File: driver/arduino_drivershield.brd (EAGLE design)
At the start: 59.7 x 54.3 mm, 35 parts, among them IC1 LB1973M, IC10 LB1973M, IC11 LB1973M, IC12 74HC14D, IC2 LB1973M, IC3 74HC14D, IC4 LB1973M, IC5 LB1973M, IC6 74HC14D, IC7 LB1973M, IC8 LB1973M, IC9 74HC14D, J1 J5MM, J2 J5MM, U1 ARDUINO_SHIELDLABEL

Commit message: autorouted
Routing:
- net V+: track 0.00 -> 136.5 mm
- net GND@2: track 11.9 -> 126.5 mm
- net GND@3: track 0.00 -> 108.7 mm
- net 5V@1: track 0.00 -> 104.2 mm, vias 0 -> 2
- net 5V: track 0.00 -> 93.3 mm, vias 0 -> 2
- net N$28: track 0.00 -> 81.6 mm, vias 0 -> 1
- net N$51: track 0.00 -> 77.6 mm, vias 0 -> 2
- net TX: track 0.00 -> 29.0 mm
- net RX: track 0.00 -> 29.0 mm
- net N$15: track 0.00 -> 23.9 mm, vias 0 -> 1
- net N$16: track 0.00 -> 23.9 mm, vias 0 -> 1
- net N$35: track 0.00 -> 22.7 mm, vias 0 -> 1
- net N$36: track 0.00 -> 22.4 mm, vias 0 -> 1
- net N$66: track 0.00 -> 20.6 mm
- net N$50: track 0.00 -> 20.6 mm
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
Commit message: seems I forgot to save the last routing
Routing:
- net GND@2: track 126.5 -> 108.2 mm
- net N$28: track 81.6 -> 73.0 mm
- net N$38: track 15.0 -> 12.0 mm
- net N$50: track 20.6 -> 18.0 mm, vias 0 -> 1
- net N$51: track 77.6 -> 79.1 mm
- net 5V: track 93.3 -> 92.7 mm

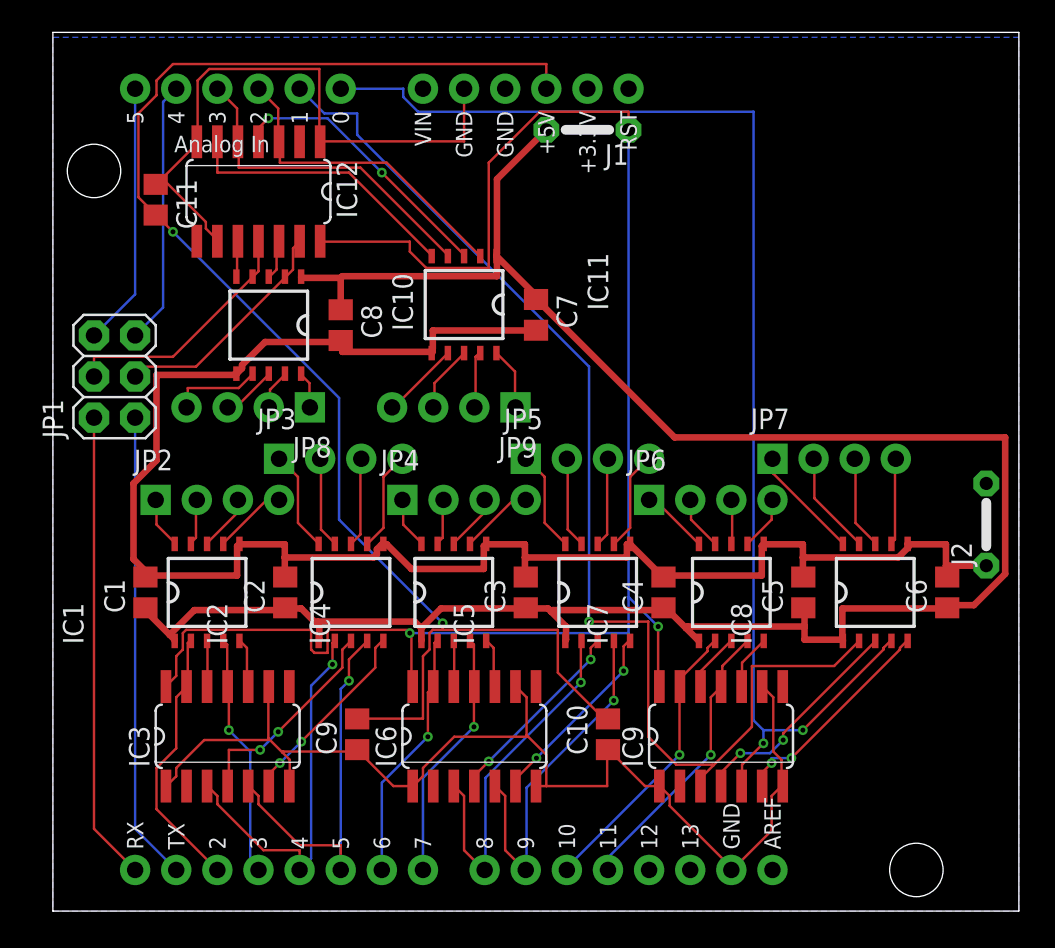
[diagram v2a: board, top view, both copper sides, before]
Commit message: added some more jumper to hopefully get better ground connections
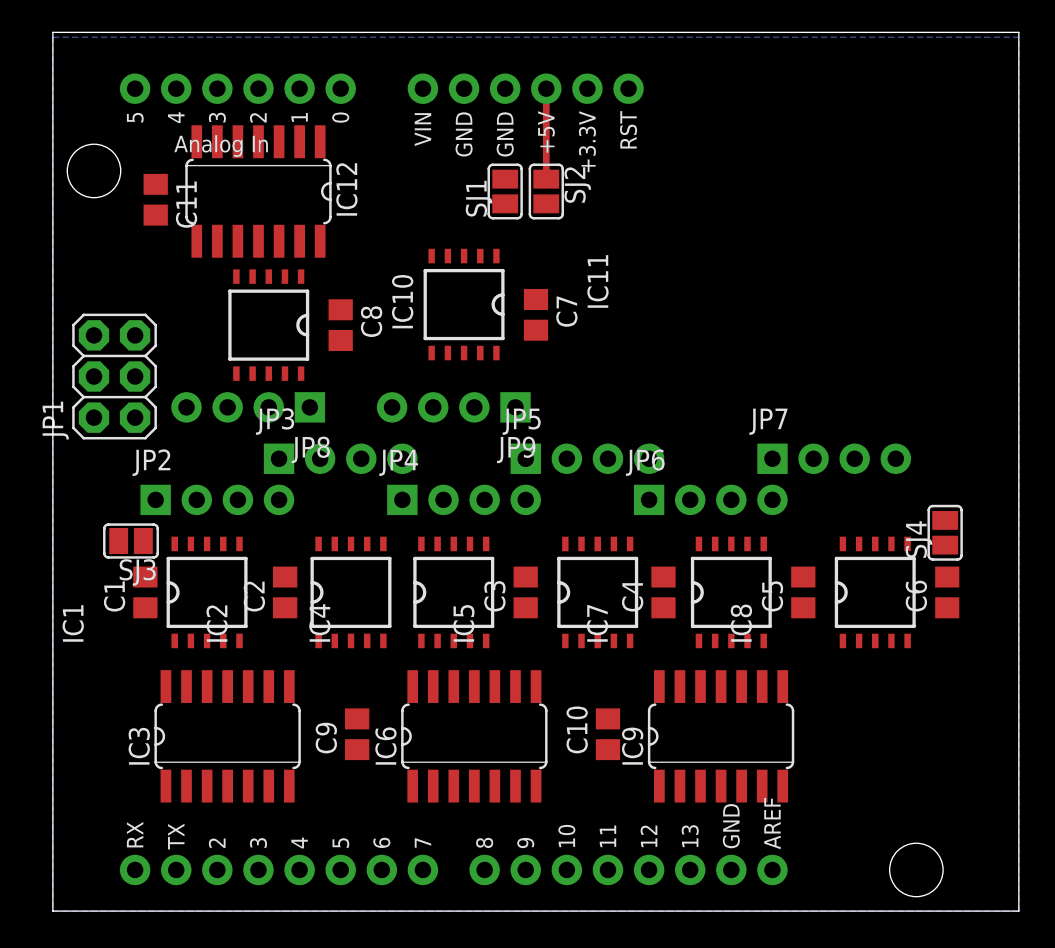
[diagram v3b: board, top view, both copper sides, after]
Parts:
- removed J1, J2: J5MM, jumper:05
- added SJ1, SJ2, SJ3, SJ4: (no value), jumper:SJ
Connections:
- removed net GND@2: C10.1, C11.1, C9.1, IC12.1, IC12.7, IC12.9, IC3.1, IC3.7, IC3.9, IC6.1, IC6.7, IC6.9, IC9.1, IC9.7, IC9.9, J2.2, U1.GND@0, U1.GND@1, U1.GND@2
- removed net GND@3: C1.2, C2.2, C3.2, C4.2, C5.2, C6.2, C7.2, C8.2, IC1.6, IC10.6, IC11.6, IC2.6, IC4.6, IC5.6, IC7.6, IC8.6, J2.1
- new net FOO: C1.2, C2.2, C3.2, C4.2, C5.2, C6.2, C7.2, C8.2, IC1.6, IC11.6, IC2.6, IC4.6, IC5.6, IC7.6, IC8.6, SJ1.1, SJ3.1, SJ4.1
- new net GND: C10.1, C11.1, C9.1, IC12.1, IC12.7, IC12.9, IC3.1, IC3.7, IC3.9, IC6.1, IC6.7, IC6.9, IC9.1, IC9.7, IC9.9, SJ1.2, U1.GND@0, U1.GND@1, U1.GND@2
- new net GND@PWR: IC10.6
- net 5V: now also SJ2.1
- net 5V@1: no longer J1.1
- net V+: now also SJ2.2; no longer J1.2
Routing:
- net V+: track 136.5 -> 0.00 mm
- net GND@3: track 108.7 -> 0.00 mm
- net GND@2: track 108.2 -> 0.00 mm
- net 5V@1: track 104.2 -> 0.00 mm, vias 2 -> 0
- net 5V: track 92.7 -> 5.59 mm, vias 2 -> 0
- net N$51: track 79.1 -> 0.00 mm, vias 2 -> 0
- net N$28: track 73.0 -> 0.00 mm, vias 1 -> 0
- net TX: track 29.0 -> 0.00 mm
- net RX: track 29.0 -> 0.00 mm
- net N$15: track 23.9 -> 0.00 mm, vias 1 -> 0
- net N$16: track 23.9 -> 0.00 mm, vias 1 -> 0
- net N$35: track 22.7 -> 0.00 mm, vias 1 -> 0
- net N$36: track 22.4 -> 0.00 mm, vias 1 -> 0
- net N$66: track 20.6 -> 0.00 mm
- net N$30: track 19.9 -> 0.00 mm
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- added copper zone on layer 16, net GND
- removed copper zone on layer 16, net GND@2

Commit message: thicker trace from 5V to power net v+, better placement for one jumper
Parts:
- moved SJ1 11.0 mm to (30.7, 33.8), turned to 0 degrees
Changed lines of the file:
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@@
 <element name="C10" library="rcl" package="C0805" value="" x="34.29" y="10.922" rot="R90"/>
 <element name="C11" library="rcl" package="C0805" value="" x="6.35" y="43.942" rot="R270"/>
-<element name="SJ1" library="jumper" package="SJ" value="" x="27.94" y="44.45" rot="R90"/>
+<element name="SJ1" library="jumper" package="SJ" value="" x="30.734" y="33.782"/>
 <element name="SJ2" library="jumper" package="SJ" value="" x="30.48" y="44.45" rot="R270"/>
 <element name="SJ3" library="jumper" package="SJ" value="" x="4.826" y="22.86" rot="R180"/>
@@
 <wire x1="17.78" y1="35.245" x2="23.4" y2="34.469" width="0" layer="19" extent="1-1"/>
 <wire x1="29.845" y1="35.88" x2="23.4" y2="34.469" width="0" layer="19" extent="1-1"/>
-<wire x1="27.94" y1="43.688" x2="29.845" y2="35.88" width="0" layer="19" extent="1-1"/>
+<wire x1="29.972" y1="33.782" x2="29.845" y2="35.88" width="0" layer="19" extent="1-1"/>
 </signal>
 <signal name="GND">
@@
 <contactref element="C11" pad="1"/>
 <contactref element="SJ1" pad="2"/>
-<wire x1="27.94" y1="50.8" x2="27.94" y2="45.212" width="0" layer="19" extent="1-1"/>
+<wire x1="27.94" y1="50.8" x2="31.496" y2="33.782" width="0" layer="19" extent="1-1"/>
 <wire x1="45.085" y1="7.7216" x2="41.91" y2="2.54" width="0" layer="19" extent="1-1"/>
 <wire x1="43.815" y1="13.8684" x2="45.085" y2="7.7216" width="0" layer="19" extent="1-1"/>
@@
 <wire x1="18.796" y1="11.872" x2="6.35" y2="42.992" width="0" layer="19" extent="1-1"/>
 <wire x1="34.29" y1="11.872" x2="18.796" y2="11.872" width="0" layer="19" extent="1-1"/>
-<wire x1="30.48" y1="50.8" x2="30.48" y2="45.212" width="0.4064" layer="1"/>
+<wire x1="30.48" y1="50.8" x2="30.48" y2="45.212" width="0.6096" layer="1"/>
 </signal>
 <signal name="GND@PWR" class="1">

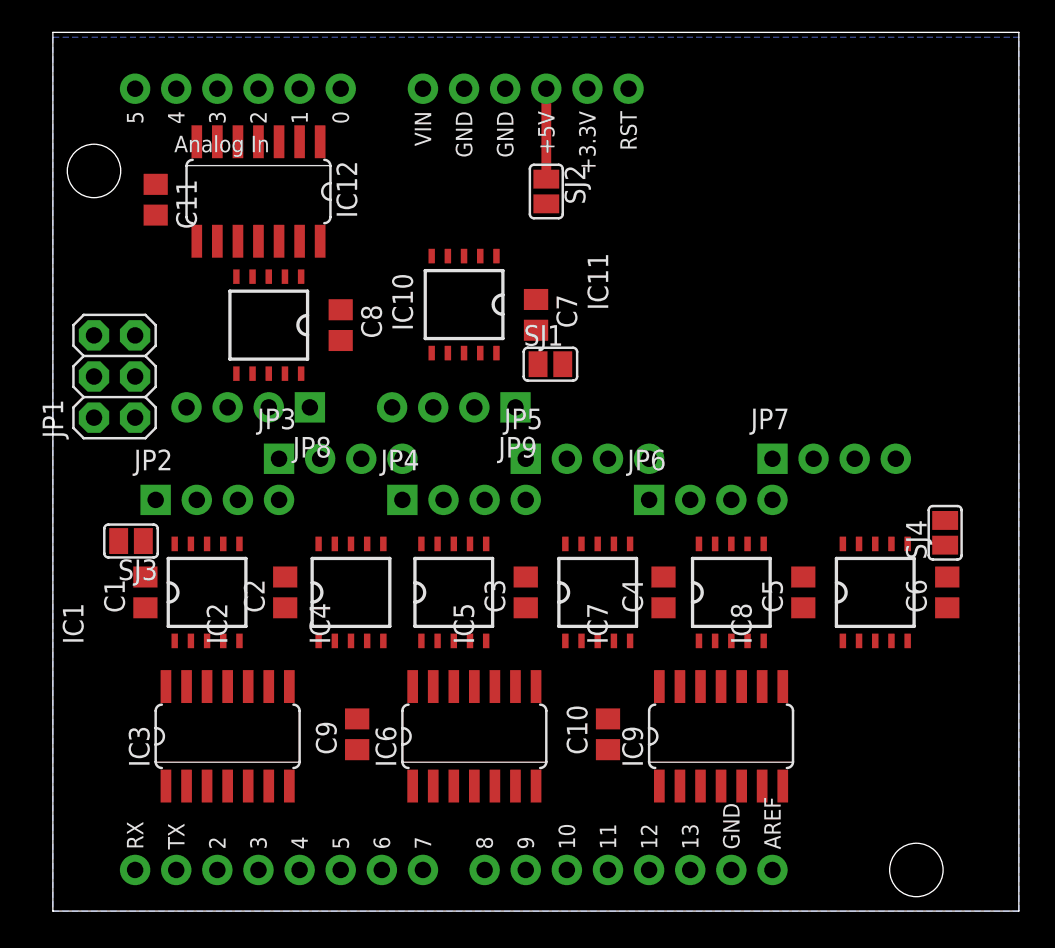
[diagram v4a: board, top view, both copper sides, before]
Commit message: realized the GND jumpers should probably be at bottom side
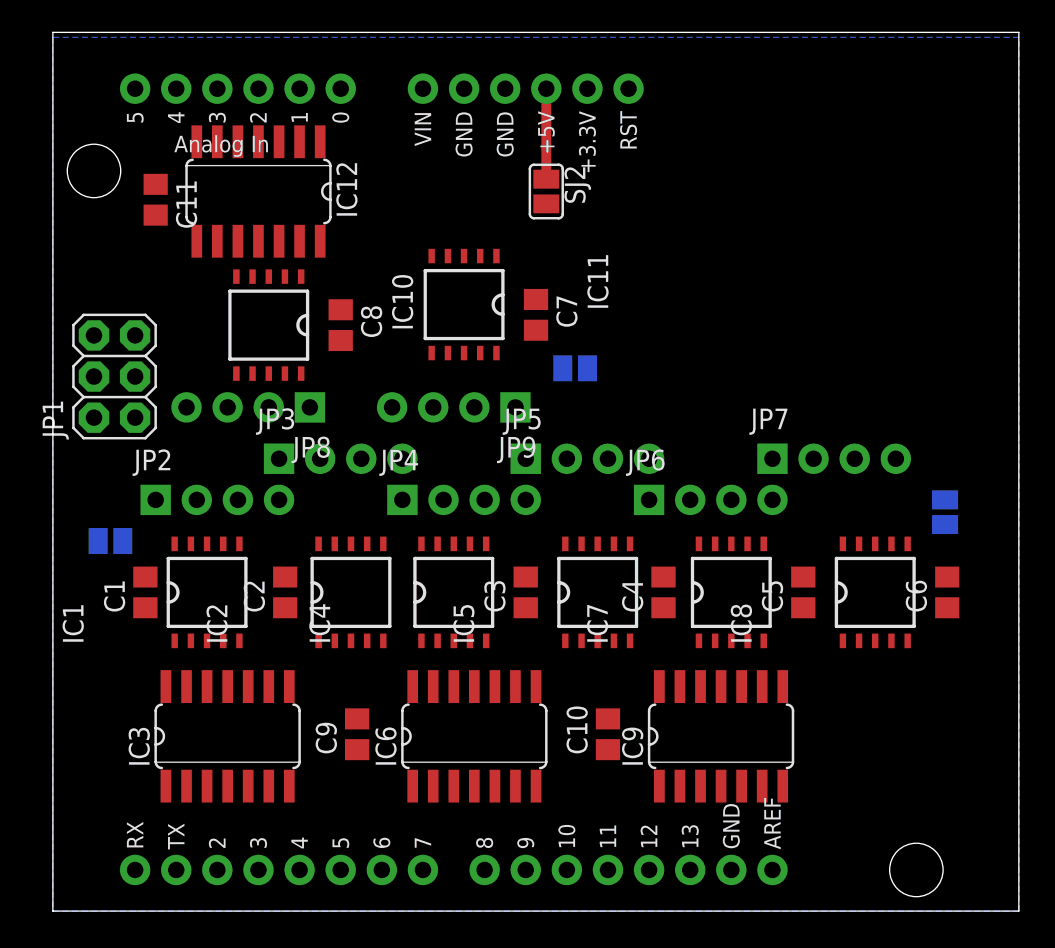
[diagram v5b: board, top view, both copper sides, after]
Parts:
- moved SJ1 1.55 mm to (32.3, 33.5), flipped to the bottom, turned to 180 degrees
- moved SJ4 1.27 mm to (55.1, 24.6), flipped to the bottom
- moved SJ3 1.27 mm to (3.56, 22.9), flipped to the bottom, turned to 0 degrees
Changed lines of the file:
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@@
 <element name="C10" library="rcl" package="C0805" value="" x="34.29" y="10.922" rot="R90"/>
 <element name="C11" library="rcl" package="C0805" value="" x="6.35" y="43.942" rot="R270"/>
-<element name="SJ1" library="jumper" package="SJ" value="" x="30.734" y="33.782"/>
+<element name="SJ1" library="jumper" package="SJ" value="" x="32.258" y="33.528" rot="MR180"/>
 <element name="SJ2" library="jumper" package="SJ" value="" x="30.48" y="44.45" rot="R270"/>
-<element name="SJ3" library="jumper" package="SJ" value="" x="4.826" y="22.86" rot="R180"/>
-<element name="SJ4" library="jumper" package="SJ" value="" x="55.118" y="23.368" rot="R90"/>
+<element name="SJ3" library="jumper" package="SJ" value="" x="3.556" y="22.86" rot="MR0"/>
+<element name="SJ4" library="jumper" package="SJ" value="" x="55.118" y="24.638" rot="MR90"/>
 </elements>
 <signals>
@@
 <contactref element="SJ3" pad="1"/>
 <contactref element="SJ4" pad="1"/>
-<wire x1="55.245" y1="20.635" x2="55.118" y2="22.606" width="0" layer="19" extent="1-1"/>
-<wire x1="52.8" y1="22.681" x2="55.245" y2="20.635" width="0" layer="19" extent="1-1"/>
+<wire x1="55.118" y1="23.876" x2="55.245" y2="20.635" width="0" layer="19" extent="1-1"/>
+<wire x1="52.8" y1="22.681" x2="55.118" y2="23.876" width="0" layer="19" extent="1-1"/>
 <wire x1="46.355" y1="20.635" x2="52.8" y2="22.681" width="0" layer="19" extent="1-1"/>
 <wire x1="43.91" y1="22.681" x2="46.355" y2="20.635" width="0" layer="19" extent="1-1"/>
@@
 <wire x1="14.351" y1="20.635" x2="20.415" y2="22.681" width="0" layer="19" extent="1-1"/>
 <wire x1="11.525" y1="22.681" x2="14.351" y2="20.635" width="0" layer="19" extent="1-1"/>
-<wire x1="5.588" y1="22.86" x2="11.525" y2="22.681" width="0" layer="19" extent="1-1"/>
-<wire x1="5.715" y1="20.635" x2="5.588" y2="22.86" width="0" layer="19" extent="1-1"/>
-<wire x1="23.4" y1="34.469" x2="20.415" y2="22.681" width="0" layer="19" extent="1-1"/>
+<wire x1="4.318" y1="22.86" x2="11.525" y2="22.681" width="0" layer="19" extent="1-1"/>
+<wire x1="5.715" y1="20.635" x2="4.318" y2="22.86" width="0" layer="19" extent="1-1"/>
+<wire x1="31.496" y1="33.528" x2="26.765" y2="22.681" width="0" layer="19" extent="1-1"/>
+<wire x1="29.845" y1="35.88" x2="31.496" y2="33.528" width="0" layer="19" extent="1-1"/>
+<wire x1="23.4" y1="34.469" x2="29.845" y2="35.88" width="0" layer="19" extent="1-1"/>
 <wire x1="17.78" y1="35.245" x2="23.4" y2="34.469" width="0" layer="19" extent="1-1"/>
-<wire x1="29.845" y1="35.88" x2="23.4" y2="34.469" width="0" layer="19" extent="1-1"/>
-<wire x1="29.972" y1="33.782" x2="29.845" y2="35.88" width="0" layer="19" extent="1-1"/>
 </signal>
 <signal name="GND">
@@
 <contactref element="C11" pad="1"/>
 <contactref element="SJ1" pad="2"/>
-<wire x1="27.94" y1="50.8" x2="31.496" y2="33.782" width="0" layer="19" extent="1-1"/>
+<wire x1="27.94" y1="50.8" x2="33.02" y2="33.528" width="0" layer="19" extent="1-1"/>
 <wire x1="45.085" y1="7.7216" x2="41.91" y2="2.54" width="0" layer="19" extent="1-1"/>
 <wire x1="43.815" y1="13.8684" x2="45.085" y2="7.7216" width="0" layer="19" extent="1-1"/>
@@
 <contactref element="U1" pad="5V"/>
 <contactref element="SJ2" pad="1"/>
+<wire x1="30.48" y1="50.8" x2="30.48" y2="45.212" width="0.6096" layer="1"/>
 <wire x1="6.35" y1="42.992" x2="30.48" y2="45.212" width="0" layer="19" extent="1-1"/>
 <wire x1="18.796" y1="11.872" x2="6.35" y2="42.992" width="0" layer="19" extent="1-1"/>
 <wire x1="34.29" y1="11.872" x2="18.796" y2="11.872" width="0" layer="19" extent="1-1"/>
-<wire x1="30.48" y1="50.8" x2="30.48" y2="45.212" width="0.6096" layer="1"/>
 </signal>
 <signal name="GND@PWR" class="1">

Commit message: routed, the one airwire is no problem since the GND pins are connected on the arduino board
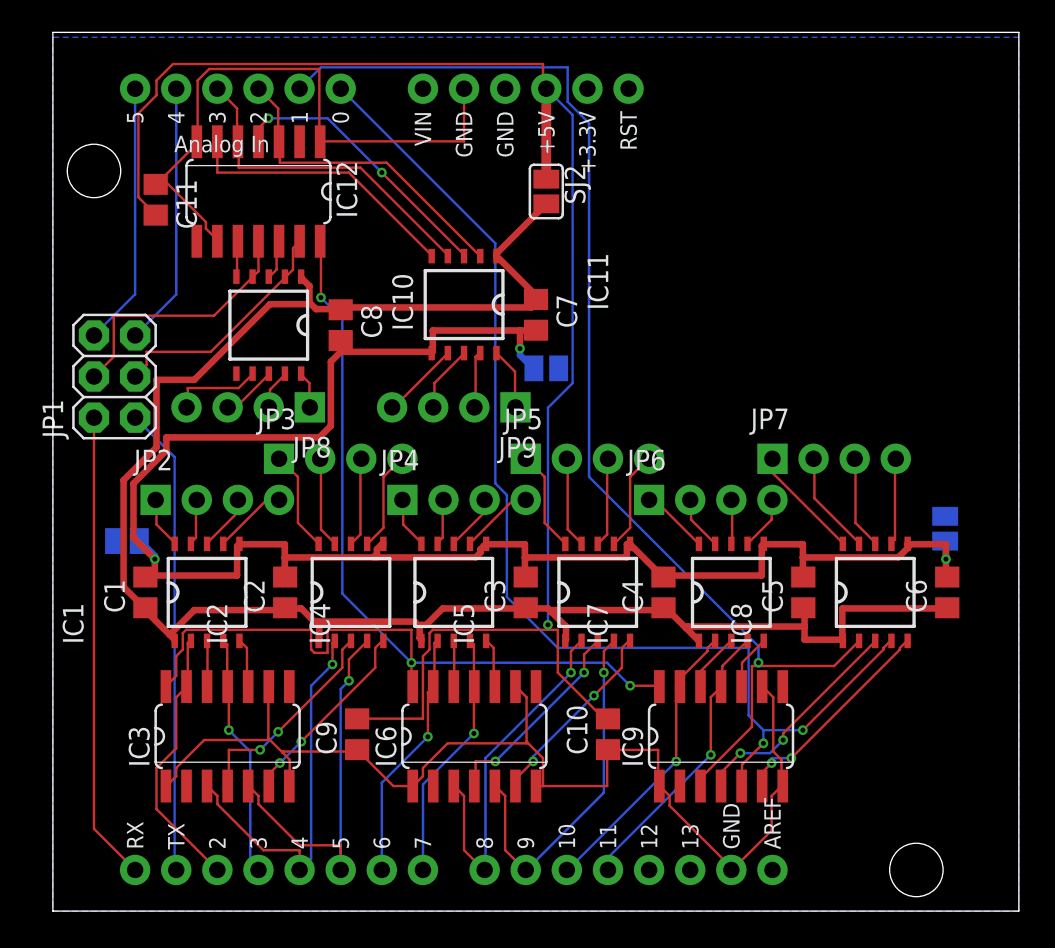
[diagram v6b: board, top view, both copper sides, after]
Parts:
- moved SJ1 1.78 mm to (30.5, 33.5)
- moved SJ4 1.02 mm to (55.1, 23.6)
- moved SJ3 1.02 mm to (4.57, 22.9)
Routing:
- net V+: track 0.00 -> 114.7 mm
- net FOO: track 0.00 -> 110.5 mm, vias 0 -> 3
- net GND: track 0.00 -> 109.3 mm
- net 5V: track 5.59 -> 99.9 mm, vias 0 -> 1
- net N$28: track 0.00 -> 75.0 mm, vias 0 -> 1
- net N$51: track 0.00 -> 71.6 mm, vias 0 -> 2
- net 5V@1: track 0.00 -> 68.4 mm, vias 0 -> 3
- net TX: track 0.00 -> 29.0 mm
- net RX: track 0.00 -> 29.0 mm
- net N$15: track 0.00 -> 23.9 mm, vias 0 -> 1
- net N$16: track 0.00 -> 23.9 mm, vias 0 -> 1
- net N$35: track 0.00 -> 22.7 mm, vias 0 -> 1
- net N$36: track 0.00 -> 22.4 mm, vias 0 -> 1
- net N$66: track 0.00 -> 20.6 mm
- net N$30: track 0.00 -> 19.9 mm
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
